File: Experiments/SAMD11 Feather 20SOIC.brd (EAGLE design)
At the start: 50.8 x 22.9 mm, 30 parts, among them IC1 ATSAMD11D14A-SSNT, J1 10118193-0001LF, Q1 DMG341, SW1 SPST_TACT-KMR2, U1 AP2112-3.3, U2 MCP73831T-2ACI/OT, X1 JSTPH, X2 2x5 0.05" SWD

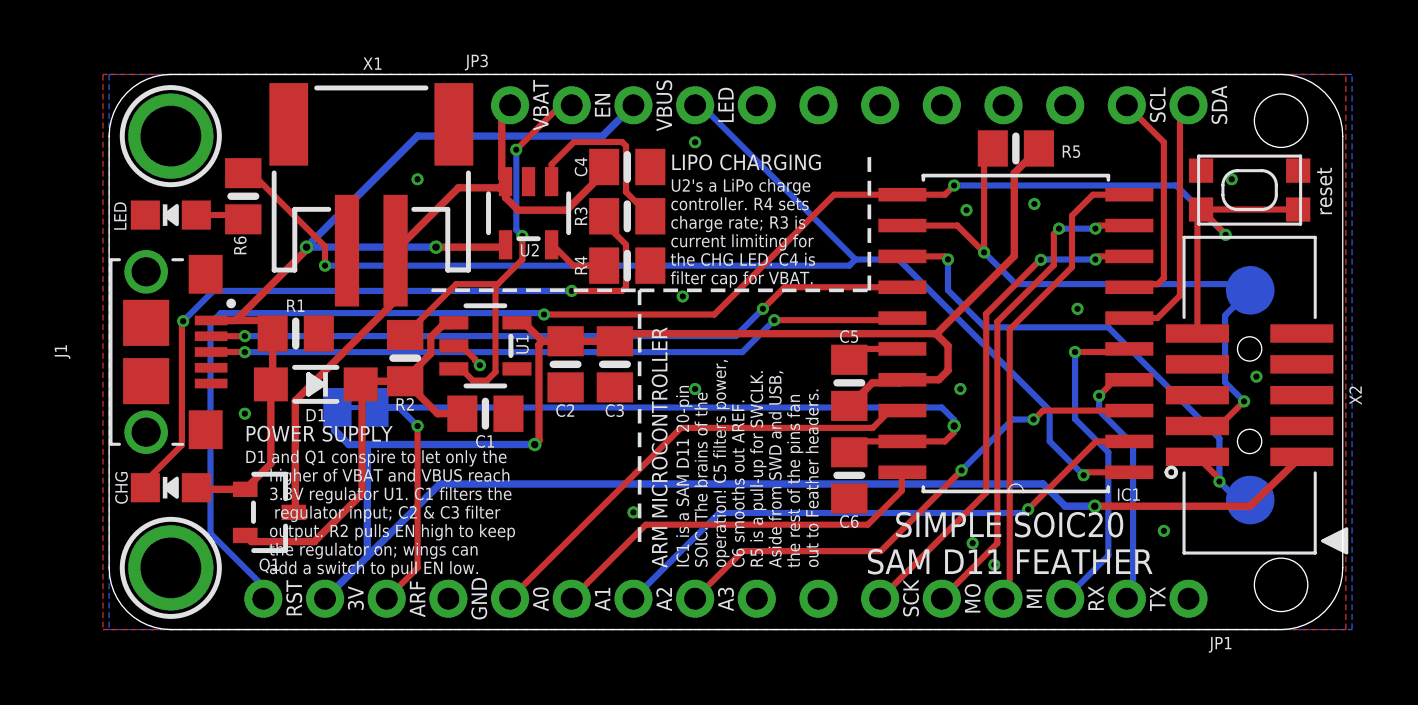
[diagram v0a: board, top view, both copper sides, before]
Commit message: fix SPI pin muxing
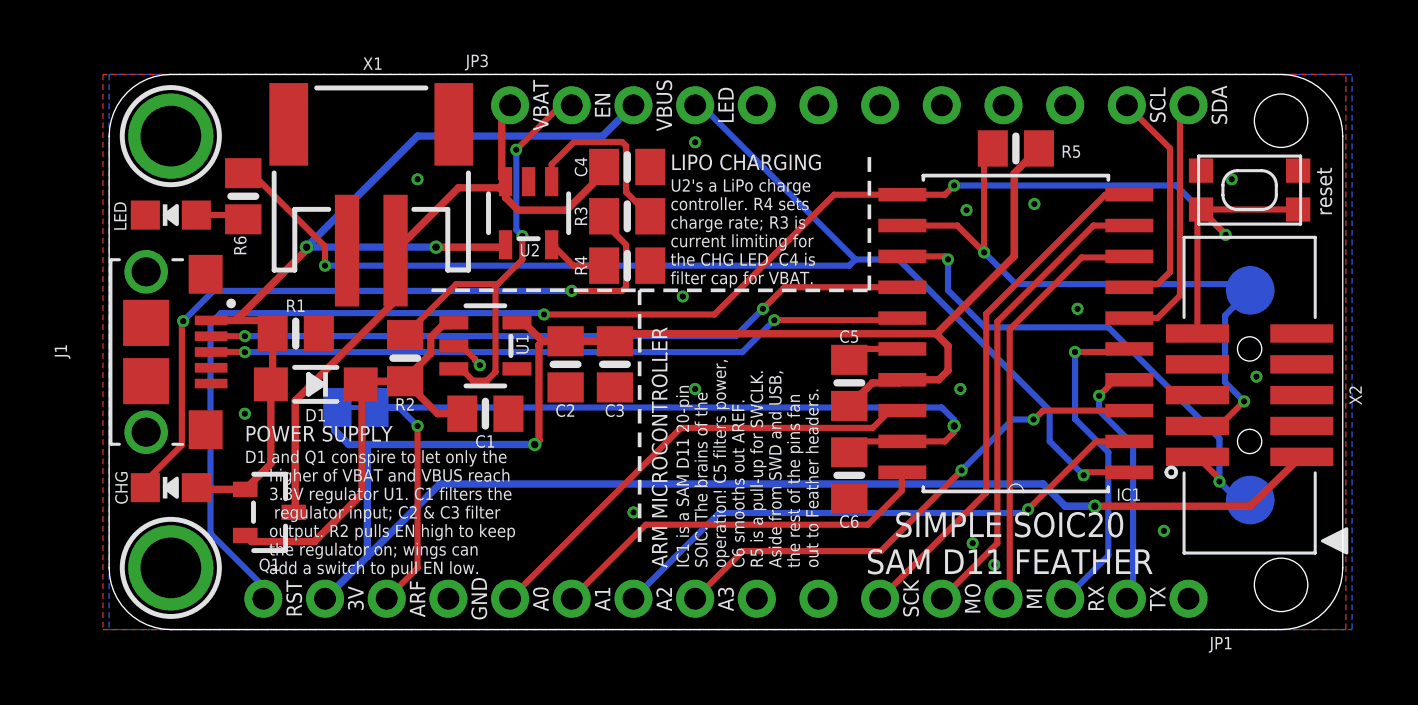
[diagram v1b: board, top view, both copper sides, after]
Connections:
- net MISO: now also IC1.8; no longer IC1.10
- net SCK: now also IC1.10; no longer IC1.8
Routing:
- net MISO: track 19.7 -> 17.4 mm
- net SCK: track 20.4 -> 21.5 mm, vias 2 -> 0
- net MOSI: track 20.2 -> 19.4 mm, vias 2 -> 0
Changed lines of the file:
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@@
 <layer number="14" name="Route14" color="1" fill="6" visible="no" active="no"/>
 <layer number="15" name="Route15" color="4" fill="6" visible="no" active="no"/>
-<layer number="16" name="Bottom" color="1" fill="1" visible="no" active="yes"/>
+<layer number="16" name="Bottom" color="1" fill="1" visible="yes" active="yes"/>
 <layer number="17" name="Pads" color="2" fill="1" visible="yes" active="yes"/>
 <layer number="18" name="Vias" color="2" fill="1" visible="yes" active="yes"/>
@@
 <wire x1="34.29" y1="1.27" x2="36.576" y2="3.556" width="0.254" layer="1"/>
 <wire x1="36.576" y1="3.556" x2="36.576" y2="12.6793875" width="0.254" layer="1"/>
-<via x="39.116" y="16.51" extent="1-16" drill="0.254"/>
-<wire x1="36.576" y1="12.6793875" x2="38.901534375" y2="15.004921875" width="0.254" layer="1"/>
-<wire x1="38.901534375" y1="16.295534375" x2="39.116" y2="16.51" width="0.254" layer="1"/>
-<wire x1="38.901534375" y1="15.004921875" x2="38.901534375" y2="16.295534375" width="0.254" layer="1"/>
-<wire x1="39.116" y1="16.51" x2="40.6146" y2="16.51" width="0.254" layer="16"/>
-<via x="40.6146" y="16.51" extent="1-16" drill="0.254"/>
-<wire x1="40.6146" y1="16.51" x2="40.7416" y2="16.637" width="0.254" layer="1"/>
-<wire x1="40.7416" y1="16.637" x2="42.0116" y2="16.637" width="0.254" layer="1"/>
+<wire x1="36.576" y1="12.6793875" x2="40.5336125" y2="16.637" width="0.254" layer="1"/>
+<wire x1="40.5336125" y1="16.637" x2="42.0116" y2="16.637" width="0.254" layer="1"/>
 </signal>
 <signal name="A5">
@@
 <wire x1="42.0116" y1="14.097" x2="42.1386" y2="14.224" width="0.254" layer="1"/>
 <wire x1="42.1386" y1="14.224" x2="43.18" y2="14.224" width="0.254" layer="1"/>
-<wire x1="43.18" y1="14.224" x2="43.434" y2="14.478" width="0.254" layer="1"/>
-<wire x1="43.434" y1="14.478" x2="43.434" y2="20.066" width="0.254" layer="1"/>
-<wire x1="43.434" y1="20.066" x2="41.91" y2="21.59" width="0.254" layer="1"/>
+<wire x1="43.18" y1="14.224" x2="43.688" y2="14.732" width="0.254" layer="1"/>
+<wire x1="43.688" y1="14.732" x2="43.688" y2="19.812" width="0.254" layer="1"/>
+<wire x1="43.688" y1="19.812" x2="41.91" y2="21.59" width="0.254" layer="1"/>
 </signal>
 <signal name="IOD">
@@
 <signal name="MISO">
 <contactref element="JP1" pad="4"/>
-<contactref element="IC1" pad="10"/>
 <wire x1="36.83" y1="1.27" x2="37.084" y2="1.524" width="0.3048" layer="1"/>
-<wire x1="37.084" y1="12.35865" x2="39.6494" y2="14.92405" width="0.254" layer="1"/>
-<wire x1="39.6494" y1="14.92405" x2="39.6494" y2="17.0434" width="0.254" layer="1"/>
-<wire x1="40.513" y1="17.907" x2="42.0116" y2="17.907" width="0.254" layer="1"/>
+<wire x1="37.084" y1="12.35865" x2="40.048675" y2="15.323325" width="0.254" layer="1"/>
 <wire x1="37.084" y1="1.524" x2="37.084" y2="12.35865" width="0.254" layer="1"/>
-<wire x1="39.6494" y1="17.0434" x2="40.513" y2="17.907" width="0.254" layer="1"/>
+<contactref element="IC1" pad="8"/>
+<wire x1="40.048675" y1="15.323325" x2="41.967925" y2="15.323325" width="0.254" layer="1"/>
+<wire x1="41.967925" y1="15.323325" x2="42.0116" y2="15.367" width="0.254" layer="1"/>
 </signal>
 <signal name="SCK">
 <contactref element="JP1" pad="6"/>
-<contactref element="IC1" pad="8"/>
 <wire x1="31.75" y1="1.27" x2="36.1188" y2="5.6388" width="0.254" layer="1"/>
-<wire x1="36.1188" y1="5.6388" x2="36.1188" y2="13.0048" width="0.254" layer="1"/>
-<wire x1="38.339865625" y1="15.225865625" x2="38.368134375" y2="15.225865625" width="0.254" layer="1"/>
-<via x="38.368134375" y="15.225865625" extent="1-16" drill="0.254"/>
-<wire x1="38.368134375" y1="15.225865625" x2="38.38226875" y2="15.24" width="0.254" layer="16"/>
-<wire x1="38.38226875" y1="15.24" x2="40.6146" y2="15.24" width="0.254" layer="16"/>
-<via x="40.6146" y="15.24" extent="1-16" drill="0.254"/>
-<wire x1="40.6146" y1="15.24" x2="40.7416" y2="15.367" width="0.254" layer="1"/>
-<wire x1="40.7416" y1="15.367" x2="42.0116" y2="15.367" width="0.254" layer="1"/>
-<wire x1="36.1188" y1="13.0048" x2="38.339865625" y2="15.225865625" width="0.254" layer="1"/>
+<wire x1="36.1188" y1="13.0048" x2="36.1188" y2="5.6388" width="0.254" layer="1"/>
+<contactref element="IC1" pad="10"/>
+<wire x1="41.021" y1="17.907" x2="36.1188" y2="13.0048" width="0.254" layer="1"/>
+<wire x1="42.0116" y1="17.907" x2="41.021" y2="17.907" width="0.254" layer="1"/>
 </signal>
 <signal name="A4">
